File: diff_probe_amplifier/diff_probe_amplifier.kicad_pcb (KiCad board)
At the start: 4 copper layers, 25.6 x 37 mm, 86 parts, among them J1 Triax_inner, J2 Triax_outer, J3 Spring+S, J4 Spring+G, J5 Spring-G, J6 Spring-S, J7 IN+, J8 IN-, SW1 GAIN, SW2 Calibrate, U1 R1283K001C, U2 OPA659, U3 OPA659, U4 OPA659, U5 MIC5225-5.0YM5, U6 ATtiny826-M, U7 MCP4451

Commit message: Revision 4
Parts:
- removed C10: 10µF, Capacitor_SMD:C_0603_1608Metric
- removed C14, C15: LXRW, oscilloscope-probes:LXRW
- removed J2: Triax_outer, oscilloscope-probes:TRIAX_OUTER_3MM
- removed R24, R25: 6.8k, Resistor_SMD:R_Array_Convex_4x0603
- removed R5: 5.1k, Resistor_SMD:R_0603_1608Metric
- removed SW2: Calibrate, Button_Switch_SMD:SW_SPST_TL3305A
- removed U5: MIC5225-5.0YM5, Package_TO_SOT_SMD:SOT-23-5
- removed U6: ATtiny826-M, Package_DFN_QFN:VQFN-20-1EP_3x3mm_P0.4mm_EP1.7x1.7mm
- removed U7: MCP4451, Package_DFN_QFN:QFN-20-1EP_4x4mm_P0.5mm_EP2.5x2.5mm
- added C16: 4.5-20pF, oscilloscope-probes:C_Trimmer_Knowles_JZ_JR, F.Cu at (92.1, 129.9)
- added C17: 4.5-20pF, oscilloscope-probes:C_Trimmer_Knowles_JZ_JR, F.Cu at (75.9, 129.9)
- added RV1: 25k, Potentiometer_SMD:Potentiometer_Bourns_3314J_Vertical, F.Cu at (84.0, 132.1)
- added RV2: 25k, Potentiometer_SMD:Potentiometer_Bourns_3314J_Vertical, F.Cu at (92.5, 144.2)
- added TP7: IN+, TestPoint:TestPoint_Pad_D2.5mm, B.Cu at (89.8, 119.2)
- added TP8: IN-, TestPoint:TestPoint_Pad_D2.5mm, B.Cu at (78.2, 119.2)
- D1, D2: value NSR05T30 -> SBR1A20
- D3: value APBD3224 -> RED; footprint oscilloscope-probes:APBD3224 -> LED_SMD:LED_0603_1608Metric
- D4, D5, D6: value PESD5V0H1BSF -> PESD5V0X1B; footprint Diode_SMD:D_0201_0603Metric -> Package_TO_SOT_SMD:SOT-23
- J1: value Triax_inner -> Conn_Triaxial; footprint oscilloscope-probes:COAX_2MM -> oscilloscope-probes:TRIAX_SOLDER
- J7, J8: footprint Connector_Coaxial:MMCX_Molex_73415-0961_Horizontal_1.6mm-PCB -> oscilloscope-probes:MMCX_Molex_73415-0961_Horizontal_1.6mm-PCB
- L1, L2, L9: value MMZ1608B601 -> BLM18KG102
- R4: value 5.1k -> 22k
- R7: value 6.8k -> 1k; footprint Resistor_SMD:R_Array_Convex_4x0603 -> Resistor_SMD:R_0603_1608Metric
- R8: value 30k -> 5.1k
- moved R8 36.9 mm to (94.0, 150.4), turned to 90 degrees
- moved R4 17.7 mm to (84.0, 114.2), turned to 180 degrees
- moved R7 14.1 mm to (87.3, 143.5), turned to 180 degrees
- moved L8 11.2 mm to (83.6, 141.2), turned to 270 degrees
- moved C13 10.5 mm to (82.1, 144.2), turned to 270 degrees
- moved D6 10.4 mm to (87.4, 146.0), turned to 270 degrees
- moved C12 8.44 mm to (80.6, 144.2), turned to 270 degrees
- moved R19 8.21 mm to (89.2, 132.5), turned to 270 degrees
- moved R18 7.71 mm to (87.7, 132.5)
- moved TP2 7.47 mm to (81.0, 144.4)
- moved TP3 7.47 mm to (87.0, 144.4)
- moved C9 7.45 mm to (82.9, 139.0), turned to 180 degrees
- moved C3 6.90 mm to (77.6, 139.9), turned to 90 degrees
- moved L6 6.86 mm to (82.1, 141.2), turned to 270 degrees
- moved L7 6.72 mm to (79.1, 141.2), turned to 270 degrees
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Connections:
- D3 pad 1: Net-(D3-Pad1) -> -6V
- R4 pad 1: Net-(R4-Pad1) -> Net-(R16-Pad2)
- R4 pad 2: +5VA -> Net-(R17-Pad2)
- R7 pad 1: Net-(R12-Pad2) -> /OFFSET_TRIM
- R7 pad 2: /DC_CMRR2 -> /OUT
- R8 pad 1: Net-(C1-Pad1) -> Net-(D3-Pad2)
- R8 pad 2: Net-(C11-Pad2) -> GNDA
- SW1 pad 1: Net-(SW1-Pad1) -> Net-(R17-Pad2)
- SW1 pad 2: Net-(R17-Pad2) -> Net-(R16-Pad2)
- SW1 pad 3: Net-(R16-Pad2) -> (no net)
- SW1 pad 4: Net-(SW1-Pad4) -> (no net)
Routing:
- net GNDA: track 5.90 -> 118.1 mm, vias 0 -> 35
- net -6V: track 16.9 -> 93.6 mm, vias 1 -> 54
- net GND: track 31.9 -> 103.3 mm, vias 20 -> 27
- net +6V: track 0.00 -> 50.7 mm, vias 0 -> 8
- net Net-(C26-Pad1): track 20.7 -> 62.3 mm, vias 3 -> 6
- net Net-(C11-Pad1): track 0.00 -> 19.5 mm
- net +5V: track 1.45 -> 20.9 mm
- net Net-(D1-Pad1): track 6.55 -> 25.8 mm
- net Net-(C1-Pad2): track 0.00 -> 18.8 mm
- net Net-(C5-Pad1): track 13.0 -> 30.7 mm, vias 0 -> 3
- net /IN-: track 0.00 -> 16.3 mm
- net /IN+: track 0.00 -> 16.3 mm
- net Net-(C19-Pad1): track 0.00 -> 14.1 mm
- net Net-(C1-Pad1): track 0.00 -> 11.4 mm
- net Net-(R17-Pad2): track 0.00 -> 8.82 mm
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- added copper zone on In1.Cu, net -6V
- added copper zone on In2.Cu, net -6V
- added copper zone on F.Cu, net GND
- added copper zone on In1.Cu, net GND
- added copper zone on B.Cu, net GNDA
- added copper zone on F.Cu, net GNDA
- added copper zone on In1.Cu, net GNDA
- added copper zone on In2.Cu, net GNDA
- removed copper zone on In2.Cu, net GND
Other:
- board size 25.6 x 37 mm -> 25.6 x 38.6 mm
- board text added: "DEDP-100 Rev 4, 8/2021"
- board text added: "https://github.com/devEmbedded/differential_probe"
- board text removed: "DEDP-100 Rev 3, 6/2021"

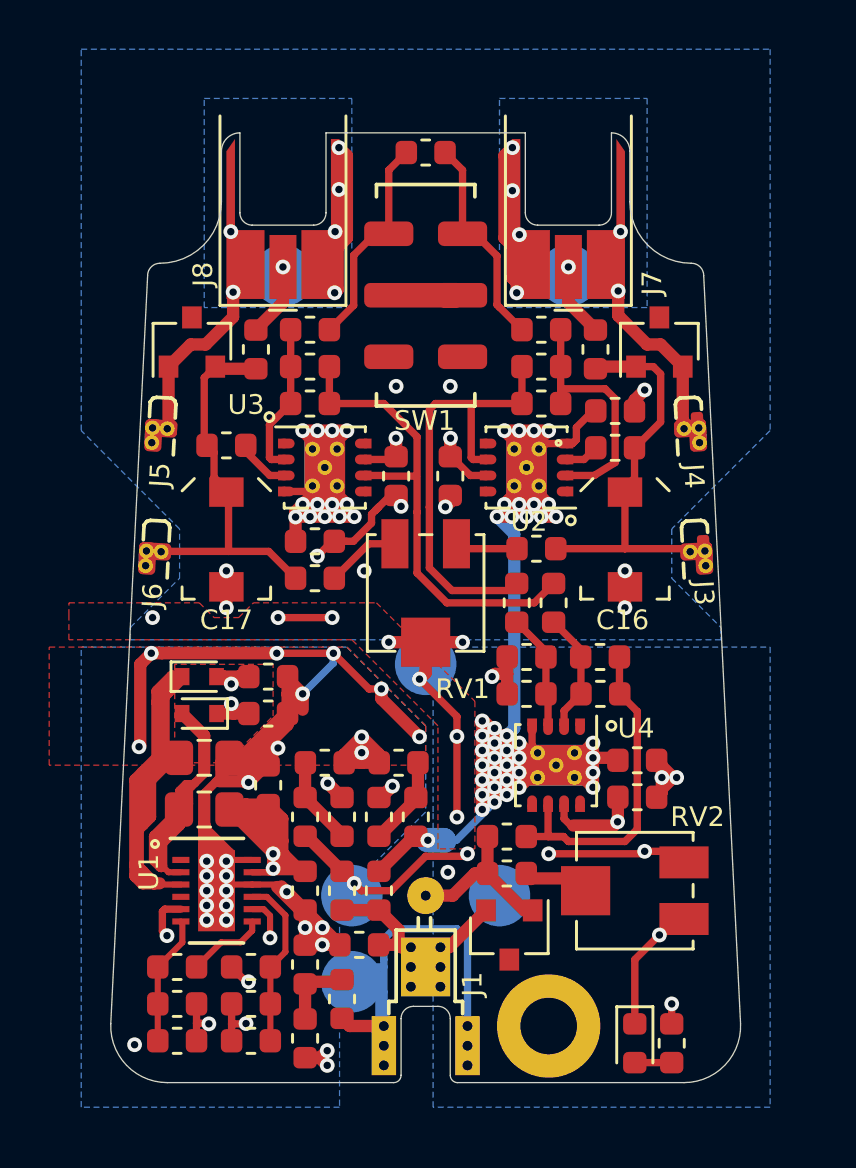
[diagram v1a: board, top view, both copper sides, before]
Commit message: Small adjustment to PCB edges after JLCPCB review failed
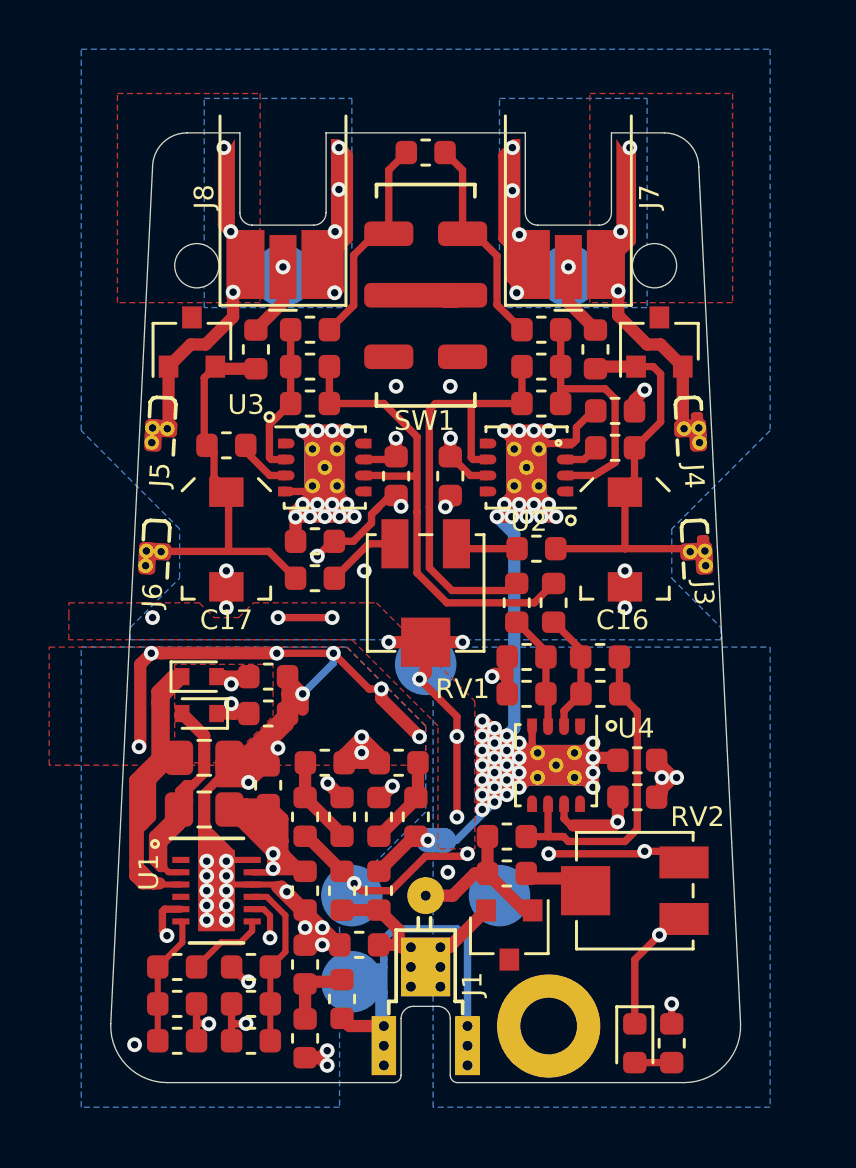
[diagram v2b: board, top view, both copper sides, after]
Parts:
- added H2: HOLE_1.8mm, oscilloscope-probes:HOLE_1.8mm, F.Cu at (93.3, 118.8)
- added H2: HOLE_1.8mm, oscilloscope-probes:HOLE_1.8mm, F.Cu at (74.7, 118.8)
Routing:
- net GNDA: track 118.1 -> 126.8 mm, vias 35 -> 37
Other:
- outline, holes or cut-outs redrawn
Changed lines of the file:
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@@
   (general
     (thickness 1.6)
-    (drawings 256)
-    (tracks 917)
+    (drawings 252)
+    (tracks 923)
     (zones 0)
-    (modules 81)
+    (modules 83)
     (nets 50)
   )
@@
     (add_net "Net-(U4-Pad8)")
   )
+  (module oscilloscope-probes:HOLE_1.8mm (layer F.Cu)
+    (at 93.3 118.8)
+    (fp_text reference H2 (at 0 0.5) (layer F.SilkS) hide
+      (effects (font (size 1 1) (thickness 0.15)))
+    )
+    (fp_text value HOLE_1.8mm (at 0 -0.5) (layer F.Fab) hide
+      (effects (font (size 1 1) (thickness 0.15)))
+    )
+    (pad "" np_thru_hole circle (at 0 0) (size 1.8 1.8) (drill 1.8) (layers *.Cu *.Mask))
+  )
+  (module oscilloscope-probes:HOLE_1.8mm (layer F.Cu)
+    (at 74.7 118.8)
+    (fp_text reference H2 (at 0 0.5) (layer F.SilkS) hide
+      (effects (font (size 1 1) (thickness 0.15)))
+    )
+    (fp_text value HOLE_1.8mm (at 0 -0.5) (layer F.Fab) hide
+      (effects (font (size 1 1) (thickness 0.15)))
+    )
+    (pad "" np_thru_hole circle (at 0 0) (size 1.8 1.8) (drill 1.8) (layers *.Cu *.Mask))
+  )
   (module oscilloscope-probes:C_Trimmer_Knowles_JZ_JR (layer F.Cu)
     (at 75.9 129.9 270)
@@
     (tags "Molex MMCX Horizontal Coaxial")
     (attr smd)
-    (fp_text reference J8 (at 2.75 3.25 270) (layer F.SilkS)
+    (fp_text reference J8 (at -0.4 3.2 270) (layer F.SilkS)
       (effects (font (size 0.8 0.8) (thickness 0.15)))
     )
@@
     (fp_line (start -4.25 -2.8) (end 4.25 -2.8) (layer F.CrtYd) (width 0.05))
     (pad 2 smd custom (at 2.35 1.525 270) (size 2.8 1.55) (layers F.Cu F.Paste F.Mask)
-      (net 38 GNDA) (zone_connect 0)
+      (net 38 GNDA) (zone_connect 2)
       (options (clearance outline) (anchor rect))
       (primitives
@@
     (tags "Molex MMCX Horizontal Coaxial")
     (attr smd)
-    (fp_text reference J7 (at 3.1 -3.4 270) (layer F.SilkS)
+    (fp_text reference J7 (at -0.4 -3.3 270) (layer F.SilkS)
       (effects (font (size 0.8 0.8) (thickness 0.15)))
     )
@@
       ))
     (pad 2 smd custom (at 2.35 -1.525 270) (size 2.8 1.55) (layers F.Cu F.Paste F.Mask)
-      (net 38 GNDA) (zone_connect 0)
+      (net 38 GNDA) (zone_connect 2)
       (options (clearance outline) (anchor rect))
       (primitives
@@
     )
   )
+  (gr_line (start 91.55 113.4) (end 93.7 113.4) (layer Edge.Cuts) (width 0.05))
+  (gr_arc (start 93.7 114.8) (end 93.7 113.4) (angle 90) (layer Edge.Cuts) (width 0.05))
+  (gr_line (start 95.1 114.8) (end 96.798006 149.60425) (layer Edge.Cuts) (width 0.05))
+  (gr_line (start 76.45 113.4) (end 74.3 113.4) (layer Edge.Cuts) (width 0.05))
+  (gr_arc (start 74.3 114.8) (end 74.3 113.4) (angle -90) (layer Edge.Cuts) (width 0.05))
   (gr_circle (center 84.8 127.2) (end 84.9 127.3) (layer B.SilkS) (width 0.12))
   (gr_circle (center 83.1 127.2) (end 83.2 127.3) (layer B.SilkS) (width 0.12))
@@
   (gr_line (start 83.5 128.1) (end 83.5 127.8) (layer B.SilkS) (width 0.12))
   (gr_poly (pts (xy 84.8 137.3) (xy 84.8 138.4) (xy 83.6 138.4) (xy 83.6 137.6) (xy 80.7 134.7) (xy 71.8 134.7) (xy 71.8 133.7) (xy 81.2 133.7)) (layer F.Mask) (width 0.05))
-  (gr_arc (start 73.2 119.2) (end 73.2 118.7) (angle -90) (layer Edge.Cuts) (width 0.05))
-  (gr_arc (start 94.8 119.2) (end 95.3 119.2) (angle -90) (layer Edge.Cuts) (width 0.05))
   (gr_circle (center 89.3 138.2) (end 89.4 138.3) (layer B.SilkS) (width 0.12))
   (gr_line (start 77.4 123.3) (end 77.2 122.9) (layer B.SilkS) (width 0.12))
@@
   (gr_line (start 89.8 120.65) (end 89.8 123.8) (layer B.SilkS) (width 0.12))
   (gr_circle (center 73 142.3) (end 73.1 142.4) (layer F.SilkS) (width 0.12))
-  (gr_text https://github.com/devEmbedded/differential_probe (at 74.4 135.45 -92.8) (layer B.SilkS)
-    (effects (font (size 0.8 0.8) (thickness 0.15)) (justify mirror))
+  (gr_text https://github.com/devEmbedded/differential_probe (at 74.5 135.7 -92.8) (layer B.SilkS)
+    (effects (font (size 0.8 0.75) (thickness 0.15)) (justify mirror))
   )
   (gr_circle (center 77.65 124.95) (end 77.8 125.05) (layer F.SilkS) (width 0.12))
@@
   (gr_line (start 83.5 148.9) (end 84.5 148.9) (layer Edge.Cuts) (width 0.05))
   (gr_line (start 83 151.7) (end 83 149.4) (layer Edge.Cuts) (width 0.05))
-  (gr_arc (start 91.55 114.15) (end 91.55 113.4) (angle 90) (layer Edge.Cuts) (width 0.05))
-  (gr_arc (start 94.8 116.2) (end 94.8 118.7) (angle 90) (layer Edge.Cuts) (width 0.05))
-  (gr_line (start 92.3 116.2) (end 92.3 114.15) (layer Edge.Cuts) (width 0.05))
-  (gr_arc (start 76.45 114.15) (end 76.45 113.4) (angle -90) (layer Edge.Cuts) (width 0.05))
   (gr_line (start 91.55 116.65) (end 91.55 113.4) (layer Edge.Cuts) (width 0.05))
   (gr_line (start 88.55 117.15) (end 91.05 117.15) (layer Edge.Cuts) (width 0.05))
@@
   (gr_line (start 76.95 117.15) (end 79.45 117.15) (layer Edge.Cuts) (width 0.05))
   (gr_line (start 76.45 113.4) (end 76.45 116.65) (layer Edge.Cuts) (width 0.05))
-  (gr_line (start 75.7 116.2) (end 75.7 114.15) (layer Edge.Cuts) (width 0.05))
-  (gr_arc (start 73.2 116.2) (end 73.2 118.7) (angle -90) (layer Edge.Cuts) (width 0.05))
   (gr_line (start 71.45 113.4) (end 112.5 113.4) (layer Dwgs.User) (width 0.01))
   (gr_text "Enclosure\nfront edge" (at 117 111.4) (layer Dwgs.User)
@@
   (gr_arc (start 73.5 149.7) (end 73.5 152) (angle 92.38594403) (layer Edge.Cuts) (width 0.05))
   (gr_arc (start 94.5 149.7) (end 94.5 152) (angle -92.38594403) (layer Edge.Cuts) (width 0.05))
-  (gr_line (start 96.798006 149.60425) (end 95.3 119.2) (layer Edge.Cuts) (width 0.05))
   (gr_line (start 73.5 152) (end 82.7 152) (layer Edge.Cuts) (width 0.05))
-  (gr_line (start 72.7 119.2) (end 71.201994 149.60425) (layer Edge.Cuts) (width 0.05))
+  (gr_line (start 72.9 114.8) (end 71.201994 149.60425) (layer Edge.Cuts) (width 0.05))
   (segment (start 76.35 139.125) (end 76.025 138.8) (width 0.5) (layer F.Cu) (net 1))
   (segment (start 75 143.7) (end 75.5 144.2) (width 0.25) (layer F.Cu) (net 1))
@@
   (segment (start 84.6 148.1) (end 84.6 146.5) (width 0.5) (layer F.Cu) (net 38))
   (segment (start 84.6 147.3) (end 83.4 147.3) (width 0.5) (layer F.Cu) (net 38))
+  (via (at 75.8 114) (size 0.6) (drill 0.3) (layers F.Cu B.Cu) (net 38))
+  (segment (start 75.8 117.135) (end 75.8 114) (width 0.5) (layer F.Cu) (net 38))
+  (segment (start 76.08 117.415) (end 75.8 117.135) (width 0.5) (layer F.Cu) (net 38))
+  (via (at 92.3 114) (size 0.6) (drill 0.3) (layers F.Cu B.Cu) (net 38))
+  (segment (start 92.3 117.775) (end 92.3 114) (width 0.5) (layer F.Cu) (net 38))
+  (segment (start 91.325 118.75) (end 92.3 117.775) (width 0.5) (layer F.Cu) (net 38))
   (segment (start 88.4125 132.5) (end 89.2 131.7125) (width 0.3) (layer F.Cu) (net 40))
   (segment (start 84.862004 132.5) (end 88.4125 132.5) (width 0.3) (layer F.Cu) (net 40))
@@
       )
     )
+  )
+  (zone (net 38) (net_name GNDA) (layer F.Cu) (hatch edge 0.508)
+    (priority 3)
+    (connect_pads yes (clearance 0.21))
+    (min_thickness 0.3)
+    (fill yes (arc_segments 32) (thermal_gap 0.31) (thermal_bridge_width 0.31))
+    (polygon
+      (pts
+        (xy 77.272298 120.3) (xy 71.472298 120.3) (xy 71.472298 111.8) (xy 77.272298 111.8)
+      )
+    )
+  )
+  (zone (net 38) (net_name GNDA) (layer F.Cu) (hatch edge 0.508)
+    (priority 3)
+    (connect_pads yes (clearance 0.21))
+    (min_thickness 0.3)
+    (fill yes (arc_segments 32) (thermal_gap 0.31) (thermal_bridge_width 0.31))
+    (polygon
+      (pts
+        (xy 96.472243 120.3) (xy 90.672243 120.3) (xy 90.672243 111.8) (xy 96.472243 111.8)
+      )
+    )
